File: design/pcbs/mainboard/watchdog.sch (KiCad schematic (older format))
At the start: 36 parts, among them K3 EC2-12NU, K4 EC2-12NU, Q1 SS8050, Q10 SS8050, Q11 SS8050, Q12 SS8050, Q2 SS8050, Q3 SS8050, Q4 SS8050, Q5 SS8550, Q6 SS8550, Q7 SS8050, Q8 SS8050, Q9 SS8050

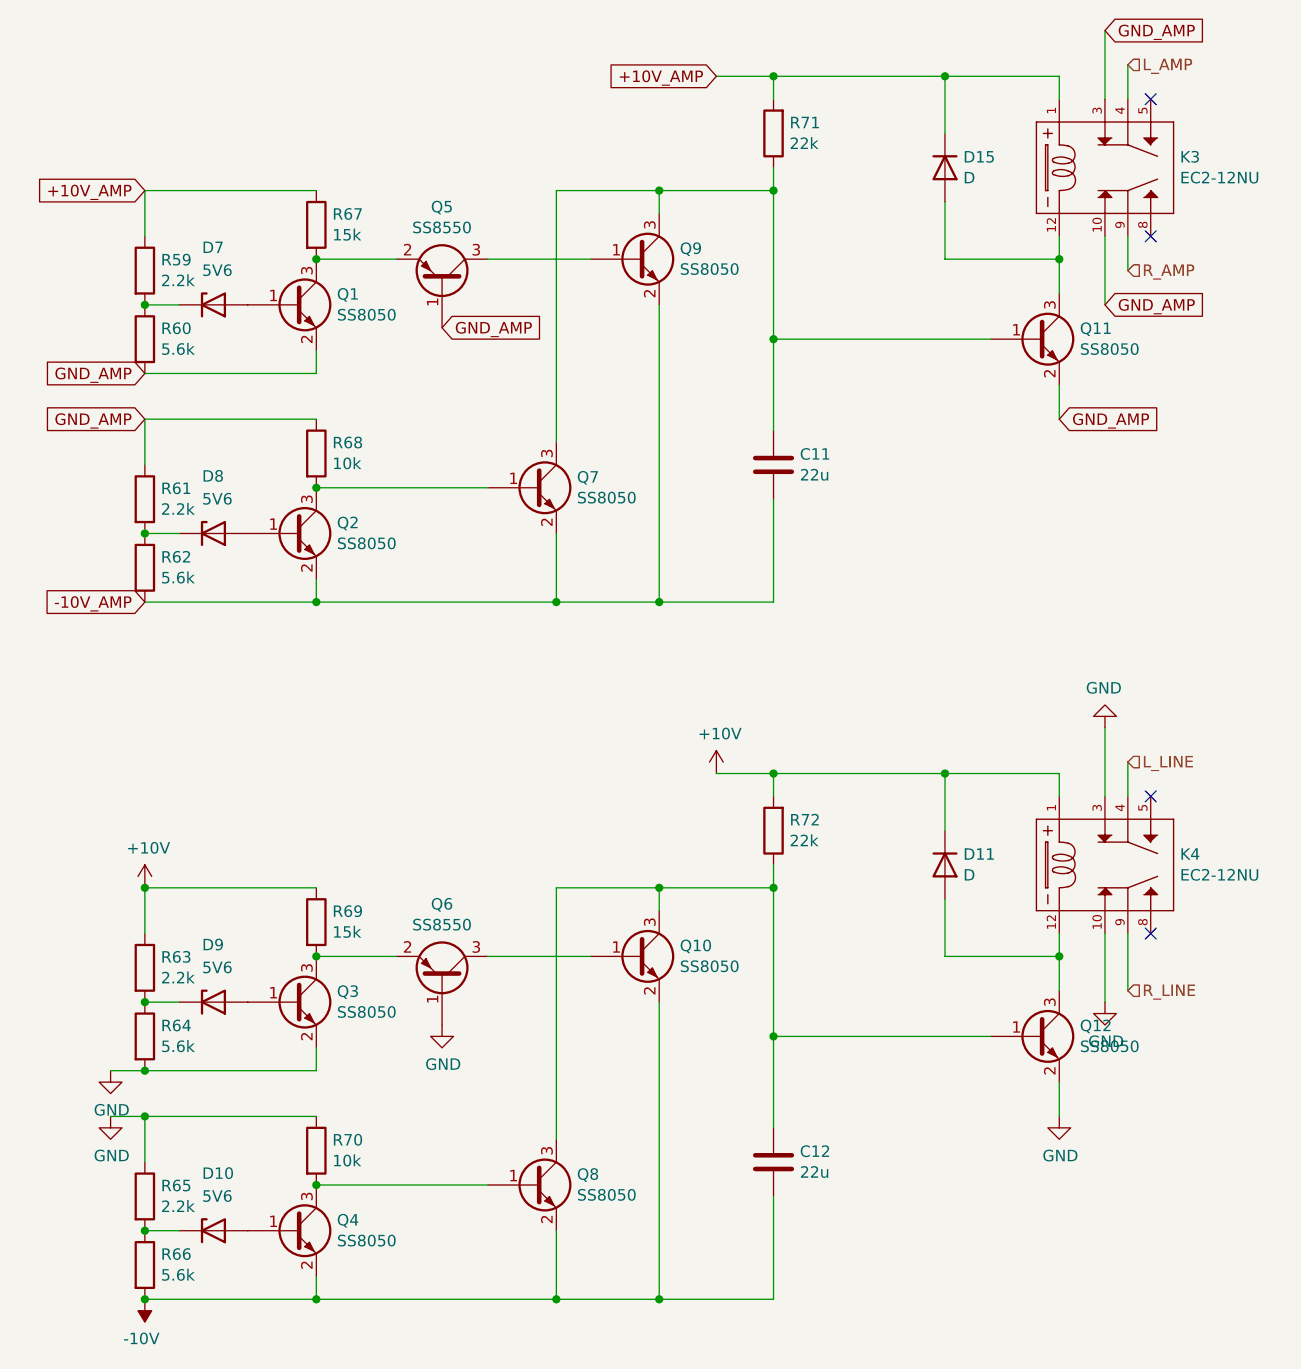
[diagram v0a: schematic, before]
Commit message: Renumbered footprints to follow board position.
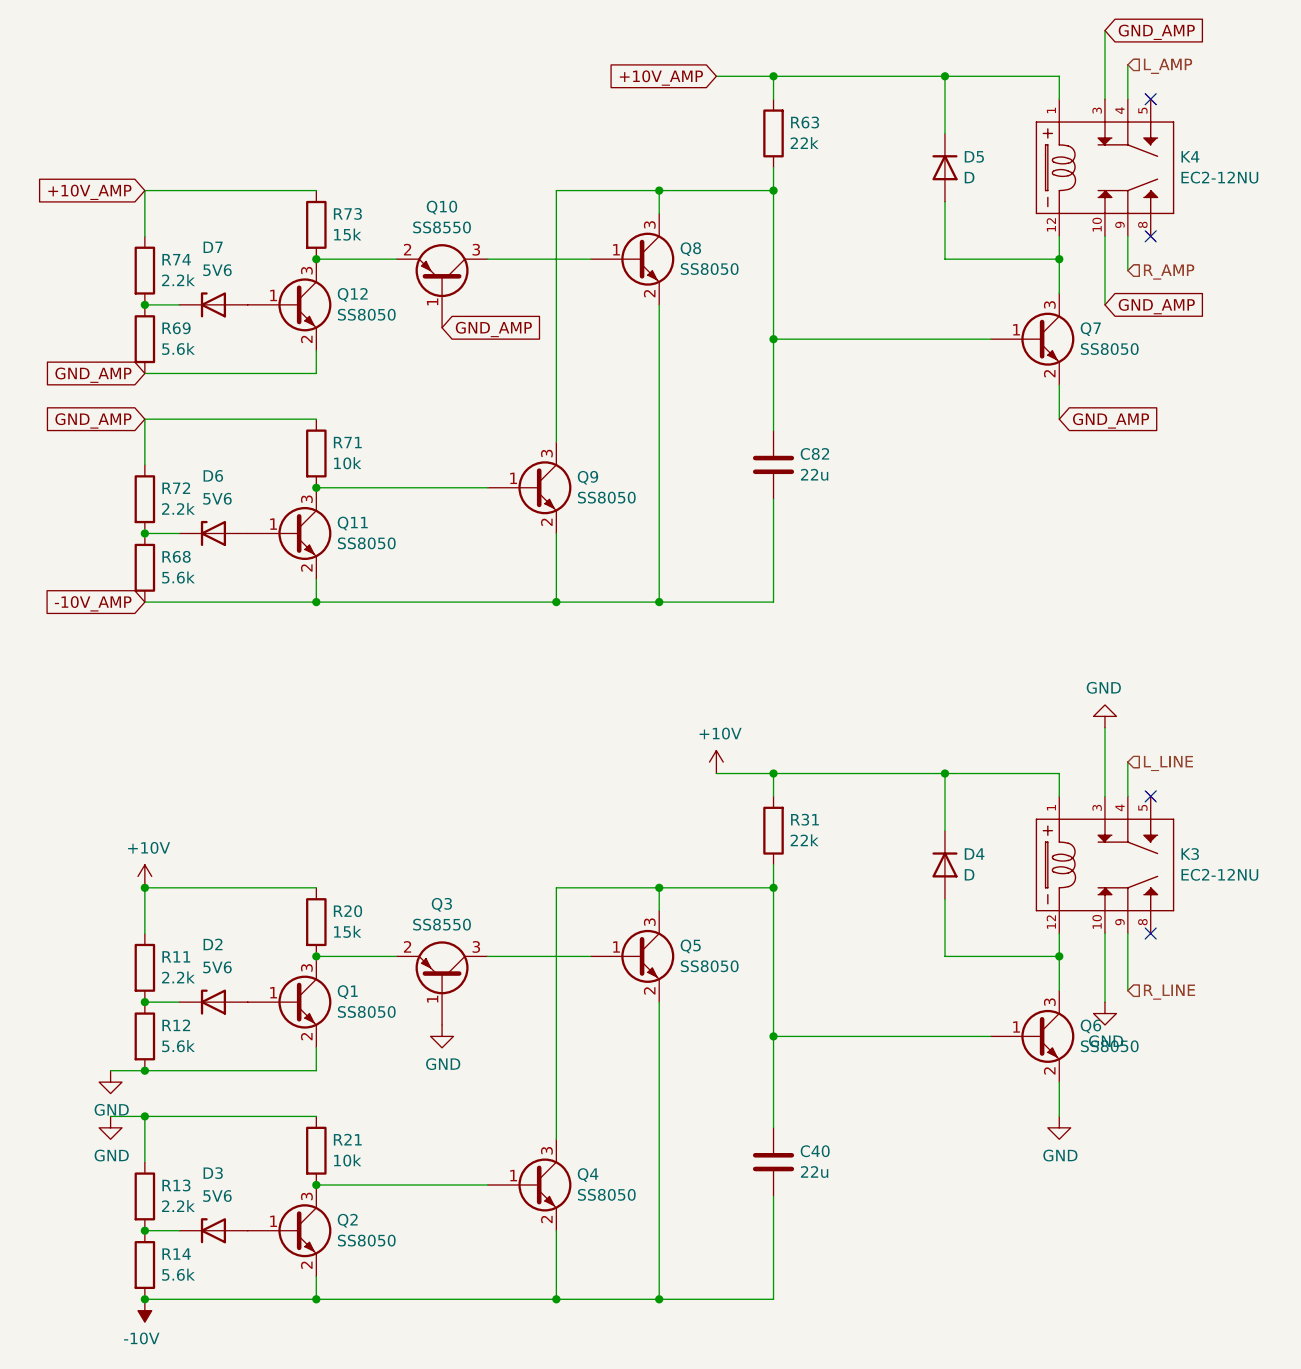
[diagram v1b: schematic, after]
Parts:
- renumbered C12 to C40, C11 to C82, D9 to D2, D10 to D3, D11 to D4, D15 to D5, D8 to D6, K4 to K3, K3 to K4, Q3 to Q1, Q5 to Q10, Q2 to Q11, Q1 to Q12, Q4 to Q2, Q6 to Q3, Q8 to Q4, Q10 to Q5, Q12 to Q6, Q11 to Q7, Q9 to Q8, Q7 to Q9, R63 to R11, R64 to R12, R65 to R13, R66 to R14, R69 to R20, R70 to R21, R72 to R31, R71 to R63, R62 to R68, R60 to R69, R68 to R71, R61 to R72, R67 to R73, R59 to R74
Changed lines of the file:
@@
 	7500 4050 7500 4150
 $Comp
-L dac:EC2-24NU K4
+L dac:EC2-24NU K3
 U 1 1 5EF22779
 P 7700 4450
-F 0 "K4" V 7654 4122 50  0000 R CNN
+F 0 "K3" V 7654 4122 50  0000 R CNN
 F 1 "EC2-12NU" V 7745 4122 50  0000 R CNN
 F 2 "RELAY_EC2-5NU" H 7700 4450 50  0001 L BNN
@@
 NoConn ~ 7900 4750
 $Comp
-L Device:R R59
+L Device:R R74
 U 1 1 5EE9C31C
 P 3500 1850
-F 0 "R59" H 3570 1896 50  0000 L CNN
+F 0 "R74" H 3570 1896 50  0000 L CNN
 F 1 "2.2k" H 3570 1805 50  0000 L CNN
 F 2 "Resistor_SMD:R_0402_1005Metric" V 3430 1850 50  0001 C CNN
@@
 $EndComp
 $Comp
-L Device:R R60
+L Device:R R69
 U 1 1 5EE9CCB7
 P 3500 2150
-F 0 "R60" H 3570 2196 50  0000 L CNN
+F 0 "R69" H 3570 2196 50  0000 L CNN
 F 1 "5.6k" H 3570 2105 50  0000 L CNN
 F 2 "Resistor_SMD:R_0402_1005Metric" V 3430 2150 50  0001 C CNN
@@
 GND_AMP
 $Comp
-L Device:Q_NPN_BEC Q1
+L Device:Q_NPN_BEC Q12
 U 1 1 5EEAE6B3
 P 4150 2000
-F 0 "Q1" H 4340 2046 50  0000 L CNN
+F 0 "Q12" H 4340 2046 50  0000 L CNN
 F 1 "SS8050" H 4340 1955 50  0000 L CNN
 F 2 "Package_TO_SOT_SMD:SOT-23" H 4350 1925 50  0001 L CIN
@@
 	3650 2000 3500 2000
 $Comp
-L Device:R R67
+L Device:R R73
 U 1 1 5EEB261C
 P 4250 1650
-F 0 "R67" H 4320 1696 50  0000 L CNN
+F 0 "R73" H 4320 1696 50  0000 L CNN
 F 1 "15k" H 4320 1605 50  0000 L CNN
 F 2 "Resistor_SMD:R_0402_1005Metric" V 4180 1650 50  0001 C CNN
@@
 $EndComp
 $Comp
-L Device:Q_PNP_BEC Q5
+L Device:Q_PNP_BEC Q10
 U 1 1 5EEBD1FE
 P 4800 1900
-F 0 "Q5" V 5128 1900 50  0000 C CNN
+F 0 "Q10" V 5128 1900 50  0000 C CNN
 F 1 "SS8550" V 5037 1900 50  0000 C CNN
 F 2 "Package_TO_SOT_SMD:SOT-23" H 5000 1825 50  0001 L CIN
@@
 Connection ~ 4250 1800
 $Comp
-L Device:D_Zener D8
+L Device:D_Zener D6
 U 1 1 5EED1B36
 P 3800 3000
-F 0 "D8" H 3750 3250 50  0000 L CNN
+F 0 "D6" H 3750 3250 50  0000 L CNN
 F 1 "5V6" H 3750 3150 50  0000 L CNN
 F 2 "Diode_SMD:D_MiniMELF" H 3800 3000 50  0001 C CNN
@@
 $EndComp
 $Comp
-L Device:R R61
+L Device:R R72
 U 1 1 5EED1B41
 P 3500 2850
-F 0 "R61" H 3570 2896 50  0000 L CNN
+F 0 "R72" H 3570 2896 50  0000 L CNN
 F 1 "2.2k" H 3570 2805 50  0000 L CNN
 F 2 "Resistor_SMD:R_0402_1005Metric" V 3430 2850 50  0001 C CNN
@@
 $EndComp
 $Comp
-L Device:R R62
+L Device:R R68
 U 1 1 5EED1B4C
 P 3500 3150
-F 0 "R62" H 3570 3196 50  0000 L CNN
+F 0 "R68" H 3570 3196 50  0000 L CNN
 F 1 "5.6k" H 3570 3105 50  0000 L CNN
 F 2 "Resistor_SMD:R_0402_1005Metric" V 3430 3150 50  0001 C CNN
@@
 $EndComp
 $Comp
-L Device:Q_NPN_BEC Q2
+L Device:Q_NPN_BEC Q11
 U 1 1 5EED1B5A
 P 4150 3000
-F 0 "Q2" H 4340 3046 50  0000 L CNN
+F 0 "Q11" H 4340 3046 50  0000 L CNN
 F 1 "SS8050" H 4340 2955 50  0000 L CNN
 F 2 "Package_TO_SOT_SMD:SOT-23" H 4350 2925 50  0001 L CIN
@@
 Connection ~ 3500 3000
 $Comp
-L Device:R R68
+L Device:R R71
 U 1 1 5EED1B69
 P 4250 2650
-F 0 "R68" H 4320 2696 50  0000 L CNN
+F 0 "R71" H 4320 2696 50  0000 L CNN
 F 1 "10k" H 4320 2605 50  0000 L CNN
 F 2 "Resistor_SMD:R_0402_1005Metric" V 4180 2650 50  0001 C CNN
@@
 	4250 3300 4250 3200
 $Comp
-L Device:Q_NPN_BEC Q7
+L Device:Q_NPN_BEC Q9
 U 1 1 5EEFD965
 P 5200 2800
-F 0 "Q7" H 5390 2846 50  0000 L CNN
+F 0 "Q9" H 5390 2846 50  0000 L CNN
 F 1 "SS8050" H 5390 2755 50  0000 L CNN
 F 2 "Package_TO_SOT_SMD:SOT-23" H 5400 2725 50  0001 L CIN
@@
 Connection ~ 4250 3300
 $Comp
-L Device:Q_NPN_BEC Q9
+L Device:Q_NPN_BEC Q8
 U 1 1 5EF05D24
 P 5650 1800
-F 0 "Q9" H 5840 1846 50  0000 L CNN
+F 0 "Q8" H 5840 1846 50  0000 L CNN
 F 1 "SS8050" H 5840 1755 50  0000 L CNN
 F 2 "Package_TO_SOT_SMD:SOT-23" H 5850 1725 50  0001 L CIN
@@
 Connection ~ 5750 1500
 $Comp
-L Device:R R71
+L Device:R R63
 U 1 1 5EF1F8B2
 P 6250 1250
-F 0 "R71" H 6180 1204 50  0000 R CNN
+F 0 "R63" H 6180 1204 50  0000 R CNN
 F 1 "22k" H 6180 1295 50  0000 R CNN
 F 2 "Resistor_SMD:R_0402_1005Metric" V 6180 1250 50  0001 C CNN
@@
 GND_AMP
 $Comp
-L dac:EC2-24NU K3
+L dac:EC2-24NU K4
 U 1 1 5EF20480
 P 7700 1400
-F 0 "K3" V 7654 1072 50  0000 R CNN
+F 0 "K4" V 7654 1072 50  0000 R CNN
 F 1 "EC2-12NU" V 7745 1072 50  0000 R CNN
 F 2 "RELAY_EC2-5NU" H 7700 1400 50  0001 L BNN
@@
 Connection ~ 7500 1800
 $Comp
-L Device:D D15
+L Device:D D5
 U 1 1 5EEBBEE1
 P 7000 1400
-F 0 "D15" V 6954 1480 50  0000 L CNN
+F 0 "D5" V 6954 1480 50  0000 L CNN
 F 1 "D" V 7045 1480 50  0000 L CNN
 F 2 "Diode_SMD:D_SOD-123F" H 7000 1400 50  0001 C CNN
@@
 	5750 1500 6250 1500
 $Comp
-L Device:D_Zener D9
+L Device:D_Zener D2
 U 1 1 5EF83CA9
 P 3800 5050
-F 0 "D9" H 3750 5300 50  0000 L CNN
+F 0 "D2" H 3750 5300 50  0000 L CNN
 F 1 "5V6" H 3750 5200 50  0000 L CNN
 F 2 "Diode_SMD:D_MiniMELF" H 3800 5050 50  0001 C CNN
@@
 $EndComp
 $Comp
-L Device:R R63
+L Device:R R11
 U 1 1 5EF83CB0
 P 3500 4900
-F 0 "R63" H 3570 4946 50  0000 L CNN
+F 0 "R11" H 3570 4946 50  0000 L CNN
 F 1 "2.2k" H 3570 4855 50  0000 L CNN
 F 2 "Resistor_SMD:R_0402_1005Metric" V 3430 4900 50  0001 C CNN
@@
 $EndComp
 $Comp
-L Device:R R64
+L Device:R R12
 U 1 1 5EF83CB7
 P 3500 5200
-F 0 "R64" H 3570 5246 50  0000 L CNN
+F 0 "R12" H 3570 5246 50  0000 L CNN
 F 1 "5.6k" H 3570 5155 50  0000 L CNN
 F 2 "Resistor_SMD:R_0402_1005Metric" V 3430 5200 50  0001 C CNN
@@
 $EndComp
 $Comp
-L Device:Q_NPN_BEC Q3
+L Device:Q_NPN_BEC Q1
 U 1 1 5EF83CBE
 P 4150 5050
-F 0 "Q3" H 4340 5096 50  0000 L CNN
+F 0 "Q1" H 4340 5096 50  0000 L CNN
 F 1 "SS8050" H 4340 5005 50  0000 L CNN
 F 2 "Package_TO_SOT_SMD:SOT-23" H 4350 4975 50  0001 L CIN
@@
 	3650 5050 3500 5050
 $Comp
-L Device:R R69
+L Device:R R20
 U 1 1 5EF83CC6
 P 4250 4700
-F 0 "R69" H 4320 4746 50  0000 L CNN
+F 0 "R20" H 4320 4746 50  0000 L CNN
 F 1 "15k" H 4320 4655 50  0000 L CNN
 F 2 "Resistor_SMD:R_0402_1005Metric" V 4180 4700 50  0001 C CNN
@@
 Connection ~ 4250 4850
 $Comp
-L Device:D_Zener D10
+L Device:D_Zener D3
 U 1 1 5EF83CD5
 P 3800 6050
-F 0 "D10" H 3750 6300 50  0000 L CNN
+F 0 "D3" H 3750 6300 50  0000 L CNN
 F 1 "5V6" H 3750 6200 50  0000 L CNN
 F 2 "Diode_SMD:D_MiniMELF" H 3800 6050 50  0001 C CNN
@@
 $EndComp
 $Comp
-L Device:R R65
+L Device:R R13
 U 1 1 5EF83CDC
 P 3500 5900
-F 0 "R65" H 3570 5946 50  0000 L CNN
+F 0 "R13" H 3570 5946 50  0000 L CNN
 F 1 "2.2k" H 3570 5855 50  0000 L CNN
 F 2 "Resistor_SMD:R_0402_1005Metric" V 3430 5900 50  0001 C CNN
@@
 $EndComp
 $Comp
-L Device:R R66
+L Device:R R14
 U 1 1 5EF83CE3
 P 3500 6200
-F 0 "R66" H 3570 6246 50  0000 L CNN
+F 0 "R14" H 3570 6246 50  0000 L CNN
 F 1 "5.6k" H 3570 6155 50  0000 L CNN
 F 2 "Resistor_SMD:R_0402_1005Metric" V 3430 6200 50  0001 C CNN
@@
 $EndComp
 $Comp
-L Device:Q_NPN_BEC Q4
+L Device:Q_NPN_BEC Q2
 U 1 1 5EF83CE9
 P 4150 6050
-F 0 "Q4" H 4340 6096 50  0000 L CNN
+F 0 "Q2" H 4340 6096 50  0000 L CNN
 F 1 "SS8050" H 4340 6005 50  0000 L CNN
 F 2 "Package_TO_SOT_SMD:SOT-23" H 4350 5975 50  0001 L CIN
@@
 Connection ~ 3500 6050
 $Comp
-L Device:R R70
+L Device:R R21
 U 1 1 5EF83CF2
 P 4250 5700
-F 0 "R70" H 4320 5746 50  0000 L CNN
+F 0 "R21" H 4320 5746 50  0000 L CNN
 F 1 "10k" H 4320 5655 50  0000 L CNN
 F 2 "Resistor_SMD:R_0402_1005Metric" V 4180 5700 50  0001 C CNN
@@
 	4250 6350 4250 6250
 $Comp
-L Device:Q_NPN_BEC Q8
+L Device:Q_NPN_BEC Q4
 U 1 1 5EF83CFF
 P 5200 5850
-F 0 "Q8" H 5390 5896 50  0000 L CNN
+F 0 "Q4" H 5390 5896 50  0000 L CNN
 F 1 "SS8050" H 5390 5805 50  0000 L CNN
 F 2 "Package_TO_SOT_SMD:SOT-23" H 5400 5775 50  0001 L CIN
@@
 Connection ~ 4250 6350
 $Comp
-L Device:Q_NPN_BEC Q10
+L Device:Q_NPN_BEC Q5
 U 1 1 5EF83D0A
 P 5650 4850
-F 0 "Q10" H 5840 4896 50  0000 L CNN
+F 0 "Q5" H 5840 4896 50  0000 L CNN
 F 1 "SS8050" H 5840 4805 50  0000 L CNN
 F 2 "Package_TO_SOT_SMD:SOT-23" H 5850 4775 50  0001 L CIN
@@
 Connection ~ 5750 4550
 $Comp
-L Device:R R72
+L Device:R R31
 U 1 1 5EF83D21
 P 6250 4300
-F 0 "R72" H 6180 4254 50  0000 R CNN
+F 0 "R31" H 6180 4254 50  0000 R CNN
 F 1 "22k" H 6180 4345 50  0000 R CNN
 F 2 "Resistor_SMD:R_0402_1005Metric" V 6180 4300 50  0001 C CNN
@@
 Connection ~ 6250 4550
 $Comp
-L Device:D D11
+L Device:D D4
 U 1 1 5EF83D37
 P 7000 4450
-F 0 "D11" V 6954 4530 50  0000 L CNN
+F 0 "D4" V 6954 4530 50  0000 L CNN
 F 1 "D" V 7045 4530 50  0000 L CNN
 F 2 "Diode_SMD:D_SOD-123F" H 7000 4450 50  0001 C CNN
@@
 Connection ~ 3500 6350
 $Comp
-L Device:Q_PNP_BEC Q6
+L Device:Q_PNP_BEC Q3
 U 1 1 5EE9455C
 P 4800 4950
-F 0 "Q6" V 5128 4950 50  0000 C CNN
+F 0 "Q3" V 5128 4950 50  0000 C CNN
 F 1 "SS8550" V 5037 4950 50  0000 C CNN
 F 2 "Package_TO_SOT_SMD:SOT-23" H 5000 4875 50  0001 L CIN
@@
 	6250 5200 7200 5200
 $Comp
-L Device:Q_NPN_BEC Q12
+L Device:Q_NPN_BEC Q6
 U 1 1 5EF83D2C
 P 7400 5200
-F 0 "Q12" H 7590 5246 50  0000 L CNN
+F 0 "Q6" H 7590 5246 50  0000 L CNN
 F 1 "SS8050" H 7590 5155 50  0000 L CNN
 F 2 "Package_TO_SOT_SMD:SOT-23" H 7600 5125 50  0001 L CIN
@@
 	7500 5550 7500 5400
 $Comp
-L Device:C C12
+L Device:C C40
 U 1 1 5EF83D16
 P 6250 5750
-F 0 "C12" H 6365 5796 50  0000 L CNN
+F 0 "C40" H 6365 5796 50  0000 L CNN
 F 1 "22u" H 6365 5705 50  0000 L CNN
 F 2 "Capacitor_SMD:C_0805_2012Metric" H 6288 5600 50  0001 C CNN
@@
 	6250 2150 7200 2150
 $Comp
-L Device:Q_NPN_BEC Q11
+L Device:Q_NPN_BEC Q7
 U 1 1 5EF29166
 P 7400 2150
-F 0 "Q11" H 7590 2196 50  0000 L CNN
+F 0 "Q7" H 7590 2196 50  0000 L CNN
 F 1 "SS8050" H 7590 2105 50  0000 L CNN
 F 2 "Package_TO_SOT_SMD:SOT-23" H 7600 2075 50  0001 L CIN
@@
 	6250 2850 6250 3300
 $Comp
-L Device:C C11
+L Device:C C82
 U 1 1 5EF12517
 P 6250 2700
-F 0 "C11" H 6365 2746 50  0000 L CNN
+F 0 "C82" H 6365 2746 50  0000 L CNN
 F 1 "22u" H 6365 2655 50  0000 L CNN
 F 2 "Capacitor_SMD:C_0805_2012Metric" H 6288 2550 50  0001 C CNN
